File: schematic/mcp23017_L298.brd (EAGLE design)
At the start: 48.6 x 49.3 mm, 12 parts, among them IC1 MEGA8-P, IC3 MCP23017SP, J1 D8_D13

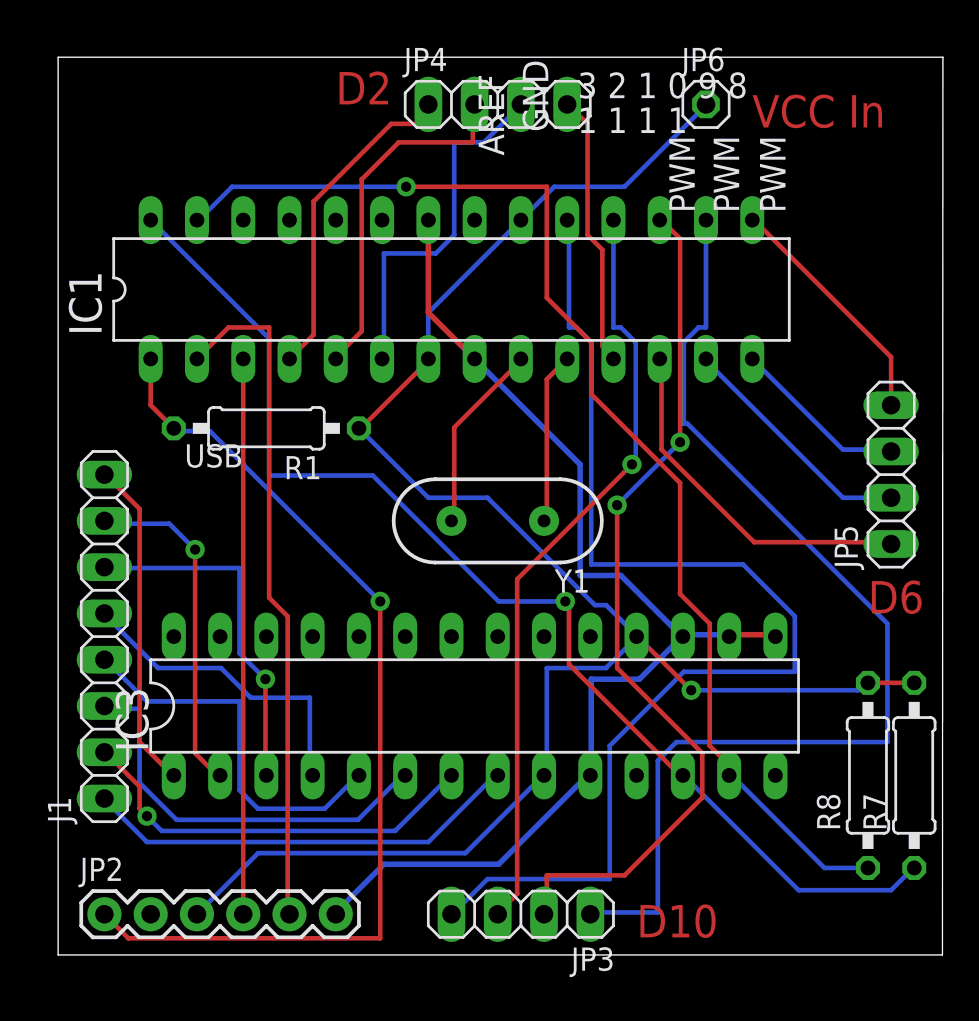
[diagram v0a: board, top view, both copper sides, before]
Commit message: v0.05
Ordered updated Schematic from Iteadstudio
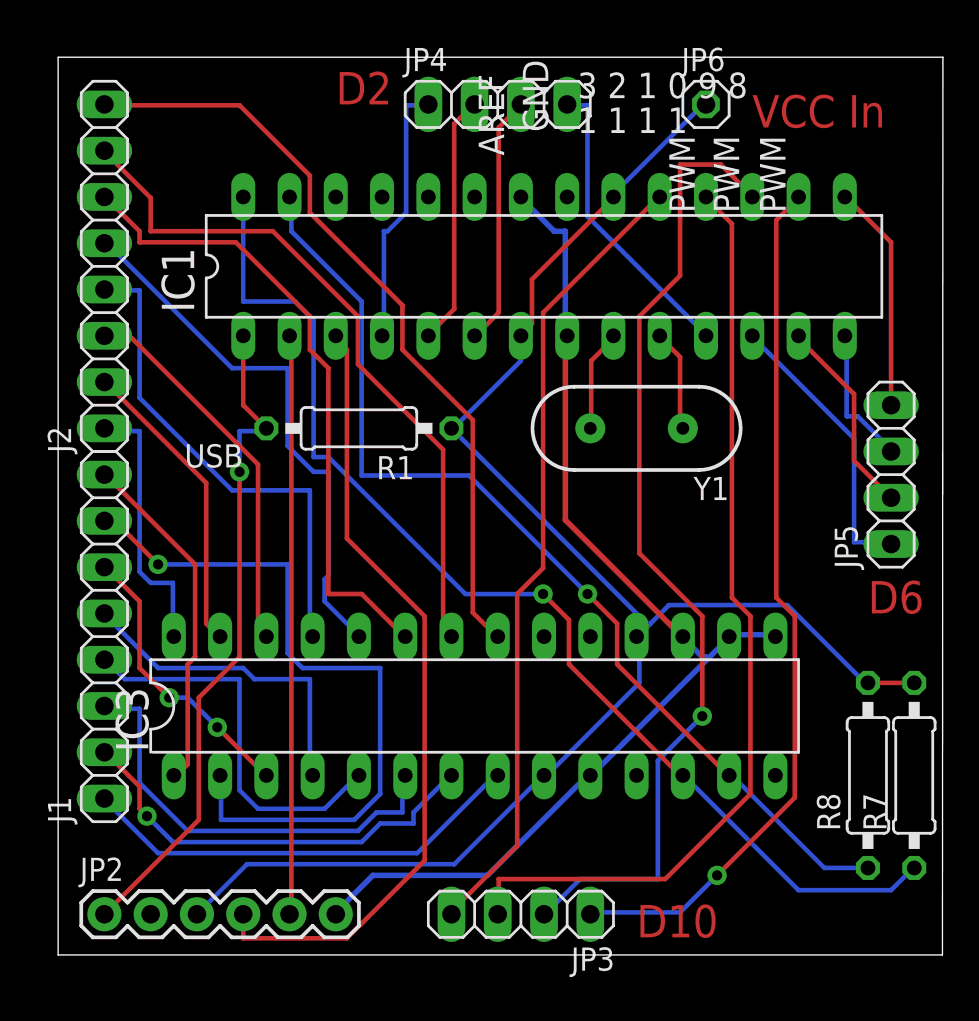
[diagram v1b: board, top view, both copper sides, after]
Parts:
- added J2: D0_D7, pinhead:1X08
- moved Y1 9.16 mm to (31.8, 29.2)
- moved IC1 5.24 mm to (26.7, 38.1)
- moved R1 5.08 mm to (16.5, 29.2)
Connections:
- new net N$12: IC3.27, J2.2
- new net N$13: IC3.26, J2.3
- new net N$14: IC3.25, J2.4
- new net N$15: IC3.24, J2.5
- new net N$16: IC3.23, J2.6
- new net N$17: IC3.22, J2.7
- new net N$18: IC3.21, J2.8
- new net N$9: IC3.28, J2.1
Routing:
- net N$18: track 0.00 -> 42.5 mm
- net N$17: track 0.00 -> 38.5 mm
- net N$16: track 0.00 -> 35.2 mm
- net N$15: track 0.00 -> 29.9 mm
- net N$14: track 0.00 -> 27.4 mm
- net N$7: track 18.7 -> 40.1 mm
- net N$13: track 0.00 -> 21.0 mm
- net D13: track 63.8 -> 44.1 mm
- net RESET: track 53.8 -> 36.8 mm
- net N$12: track 0.00 -> 16.6 mm
- net N$9: track 0.00 -> 14.8 mm
- net D1: track 30.5 -> 43.9 mm
- net D10: track 59.3 -> 47.8 mm, vias 0 -> 1
- net A4: track 66.2 -> 55.0 mm
- net VCC: track 98.6 -> 89.0 mm, vias 1 -> 0
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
